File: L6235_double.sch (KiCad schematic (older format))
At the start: 65 parts, among them J1 conn_2x16, J2 CONN_01X04, P1 CONN_01X03, P2 CONN_01X03, P4 CONN_01X02, P5 CONN_01X02, P7 CONN_01X02, P8 CONN_01X02, U1 L6235N, U2 L6235N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

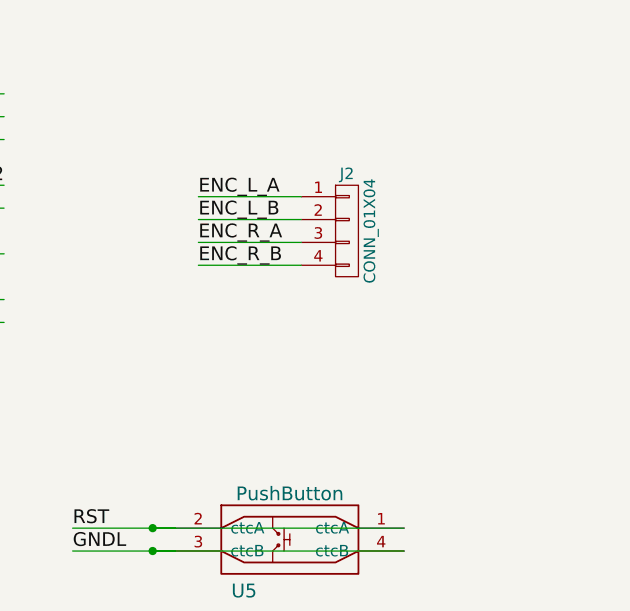
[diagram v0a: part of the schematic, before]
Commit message: changed encoder connectors
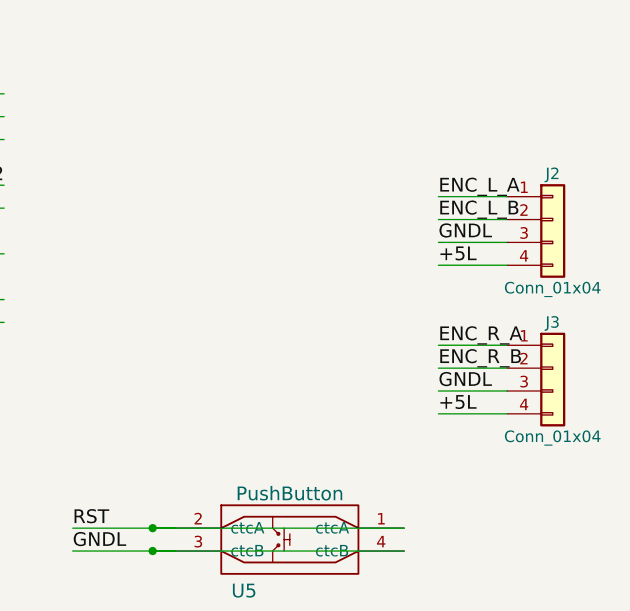
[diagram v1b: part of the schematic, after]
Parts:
- removed J2: CONN_01X04, Connectors_Molex:Molex_KK-6410-04_04x2.54mm_Straight, symbol CONN_01X04
- added J2, J3: Conn_01x04, Connectors_Molex:Molex_KK-6410-04_04x2.54mm_Straight, symbol Conn_01x04
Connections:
- wire segments 206 -> 210
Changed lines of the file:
@@
 LIBS:valves
 LIBS:L6235_double-cache
-LIBS:Libabar
 EELAYER 25 0
 EELAYER END
@@
 +5L
 $Comp
-L CONN_01X04 J2
-U 1 1 59BC3BF8
-P 13800 1650
-F 0 "J2" H 13800 1900 50  0000 C CNN
-F 1 "CONN_01X04" V 13900 1650 50  0000 C CNN
-F 2 "Connectors_Molex:Molex_KK-6410-04_04x2.54mm_Straight" H 13800 1650 50  0001 C CNN
-F 3 "" H 13800 1650 50  0001 C CNN
-	1    13800 1650
-	1    0    0    -1
-$EndComp
-Wire Wire Line
-	13600 1500 13150 1500
-Wire Wire Line
-	13600 1600 13150 1600
-Wire Wire Line
-	13600 1700 13150 1700
-Wire Wire Line
-	13600 1800 13150 1800
-Text Label 13150 1500 0    60   ~ 0
-ENC_L_A
-Text Label 13150 1600 0    60   ~ 0
-ENC_L_B
-Text Label 13150 1700 0    60   ~ 0
-ENC_R_A
-Text Label 13150 1800 0    60   ~ 0
-ENC_R_B
-$Comp
 L PushButton U5
 U 1 1 59BC90FF
@@
 Text Label 7800 2450 0    60   ~ 0
 CANL
+$Comp
+L Conn_01x04 J2
+U 1 1 5A7B2434
+P 14700 1600
+F 0 "J2" H 14700 1800 50  0000 C CNN
+F 1 "Conn_01x04" H 14700 1300 50  0000 C CNN
+F 2 "Connectors_Molex:Molex_KK-6410-04_04x2.54mm_Straight" H 14700 1600 50  0001 C CNN
+F 3 "" H 14700 1600 50  0001 C CNN
+	1    14700 1600
+	1    0    0    -1
+$EndComp
+$Comp
+L Conn_01x04 J3
+U 1 1 5A7B285B
+P 14700 2250
+F 0 "J3" H 14700 2450 50  0000 C CNN
+F 1 "Conn_01x04" H 14700 1950 50  0000 C CNN
+F 2 "Connectors_Molex:Molex_KK-6410-04_04x2.54mm_Straight" H 14700 2250 50  0001 C CNN
+F 3 "" H 14700 2250 50  0001 C CNN
+	1    14700 2250
+	1    0    0    -1
+$EndComp
+Wire Wire Line
+	14500 1500 14200 1500
+Wire Wire Line
+	14500 1600 14200 1600
+Wire Wire Line
+	14500 1700 14200 1700
+Wire Wire Line
+	14500 1800 14200 1800
+Wire Wire Line
+	14500 2150 14200 2150
+Wire Wire Line
+	14500 2250 14200 2250
+Wire Wire Line
+	14500 2350 14200 2350
+Wire Wire Line
+	14500 2450 14200 2450
+Text Label 14200 1500 0    60   ~ 0
+ENC_L_A
+Text Label 14200 1600 0    60   ~ 0
+ENC_L_B
+Text Label 14200 2150 0    60   ~ 0
+ENC_R_A
+Text Label 14200 2250 0    60   ~ 0
+ENC_R_B
+Text Label 14200 2450 0    60   ~ 0
++5L
+Text Label 14200 1800 0    60   ~ 0
++5L
+Text Label 14200 2350 0    60   ~ 0
+GNDL
+Text Label 14200 1700 0    60   ~ 0
+GNDL
 $EndSCHEMATC
